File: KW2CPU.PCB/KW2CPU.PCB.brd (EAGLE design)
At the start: 31 x 17 mm, 25 parts, among them IC1 AT45DB161D8S1

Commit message: LasCon, KW2 Frontend
Exported LasCon for Jeff, made "wide" version for milling test.
Schematic for KW2 front end in progress, missing F and ant connector.
Updated KW2 and GW libs with frontend parts
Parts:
- added C$10, C$9, L$6, R$4, R$5, R$7, R$8: (no value), GW-devices:RF-L0201
- added C$13, C$15, C$16, C$18, C$20, C$21, C$22, C$24, L$11, L$14, L$17, R$12, R$19, R$23: (no value), GW-devices:RFMD0402
- added U$3: RF6555, KW2:RF6555
- moved U$1 13.6 mm to (51.6, 37.1)
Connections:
- new net N$19: R$7.P$2, U$3.P$5
- new net N$2: R$5.P$1, U$1.P$49
- new net N$20: R$8.P$2, U$3.P$6
- new net N$21: C$13.P$1, L$14.P$1, U$3.P$15
- new net N$22: C$10.P$1, C$9.P$2, L$11.P$1, U$3.P$10, U$3.P$8
- new net N$23: C$15.P$1, L$14.P$2
- new net N$24: C$18.P$1, L$17.P$2, U$3.P$17
- new net N$25: C$16.P$1, L$17.P$1
- new net N$26: R$19.P$2, U$1.P$44
- new net N$27: C$20.P$2, R$19.P$1, U$3.P$20
- new net N$29: R$12.P$1, U$3.P$23
- new net N$3: R$4.P$1, U$1.P$50
- new net N$30: C$24.P$1, R$23.P$1, U$1.P$46, U$3.P$2
- new net N$31: C$22.P$2, U$1.P$47, U$3.P$24
- new net N$4: L$6.P$2, R$4.P$2, R$7.P$1
- new net N$5: L$6.P$1, R$5.P$2, R$8.P$1
- net +3V3: now also C$21.P$1, L$11.P$2, U$3.P$22
- net GND: now also C$10.P$2, C$13.P$2, C$15.P$2, C$16.P$2, C$18.P$2, C$20.P$1, C$21.P$2, C$22.P$1, C$24.P$2, C$9.P$1, R$12.P$2, U$3.P$1, U$3.P$12, U$3.P$13, U$3.P$14, U$3.P$16, U$3.P$18, U$3.P$19, U$3.P$3, U$3.P$7, U$3.P$9
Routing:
- net +3V3: track 33.3 -> 0.00 mm
- net GND: track 28.2 -> 0.00 mm
- net N$14: track 20.8 -> 0.00 mm
- net N$10: track 11.8 -> 0.00 mm
- net N$7: track 9.85 -> 0.00 mm
- net CLKM1: track 9.62 -> 0.00 mm
- net N$18: track 9.49 -> 0.00 mm
- net N$16: track 6.98 -> 0.00 mm
- net N$13: track 19.8 -> 14.4 mm, vias 1 -> 0
- net N$17: track 4.81 -> 0.00 mm
- net N$6: track 4.15 -> 0.00 mm
- net CLKM2: track 4.05 -> 0.00 mm
- net N$8: track 3.74 -> 0.00 mm
- net N$12: track 16.8 -> 14.4 mm, vias 1 -> 0
- net N$9: track 2.41 -> 0.00 mm
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
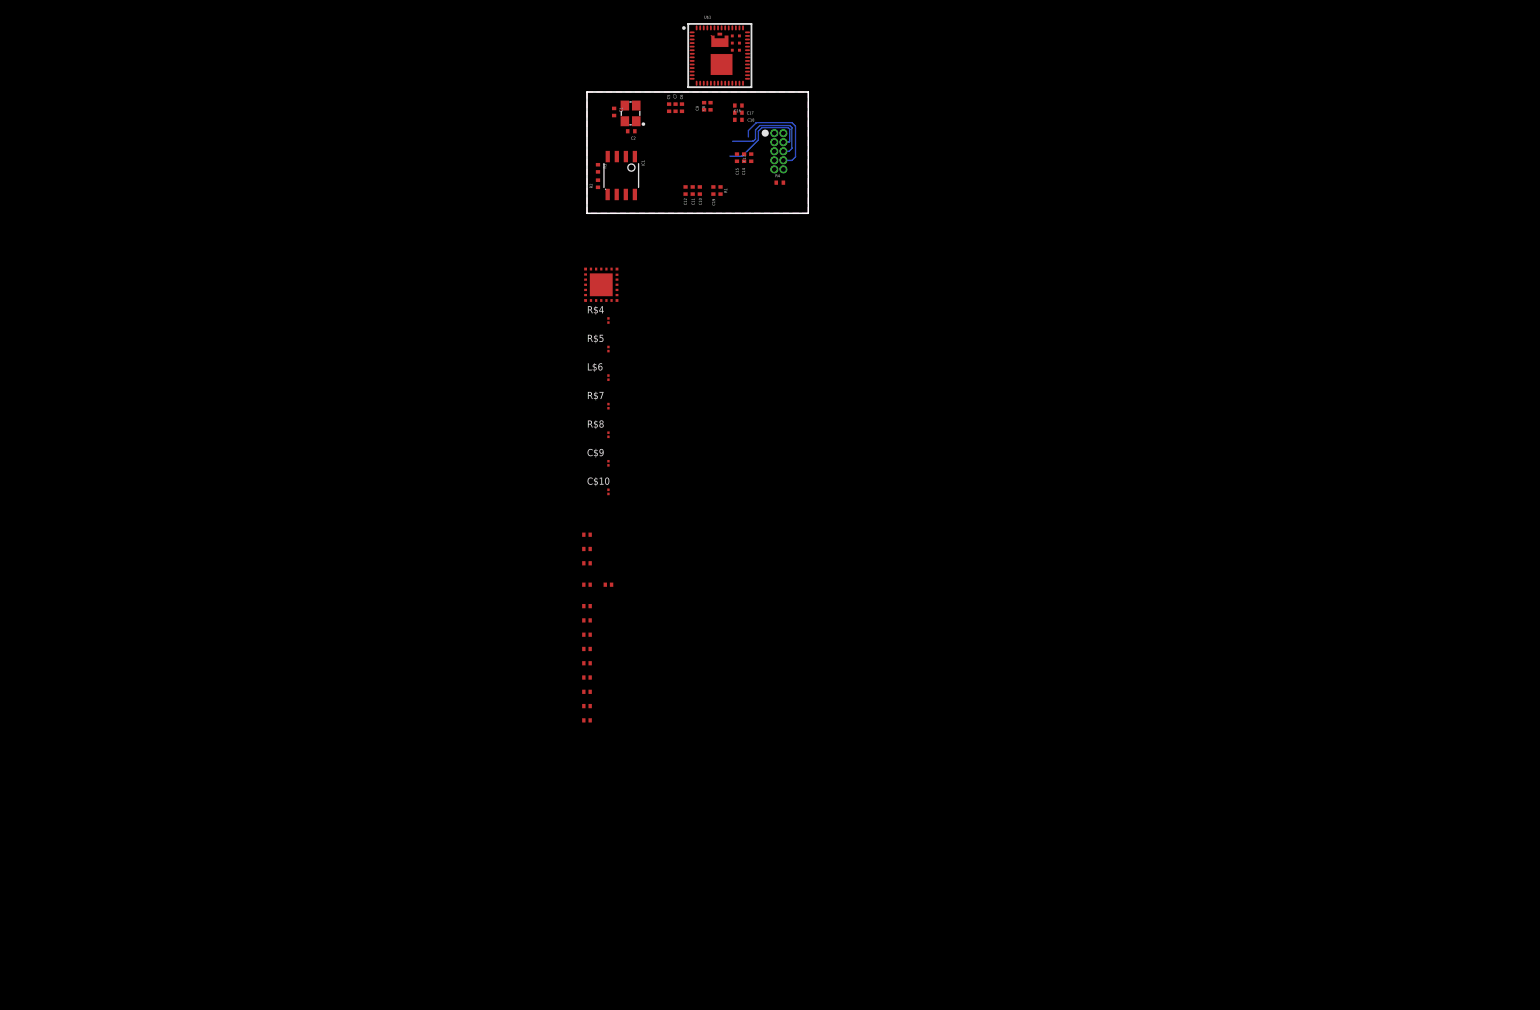
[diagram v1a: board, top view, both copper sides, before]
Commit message: KW2 antenna, LasCon panel, PosCon fiducials
Added vertical MMCX connector to KW2 design & library; added panelized
version of LasCon (old and new design); added Adafruit library and
fiducials to new PosCon
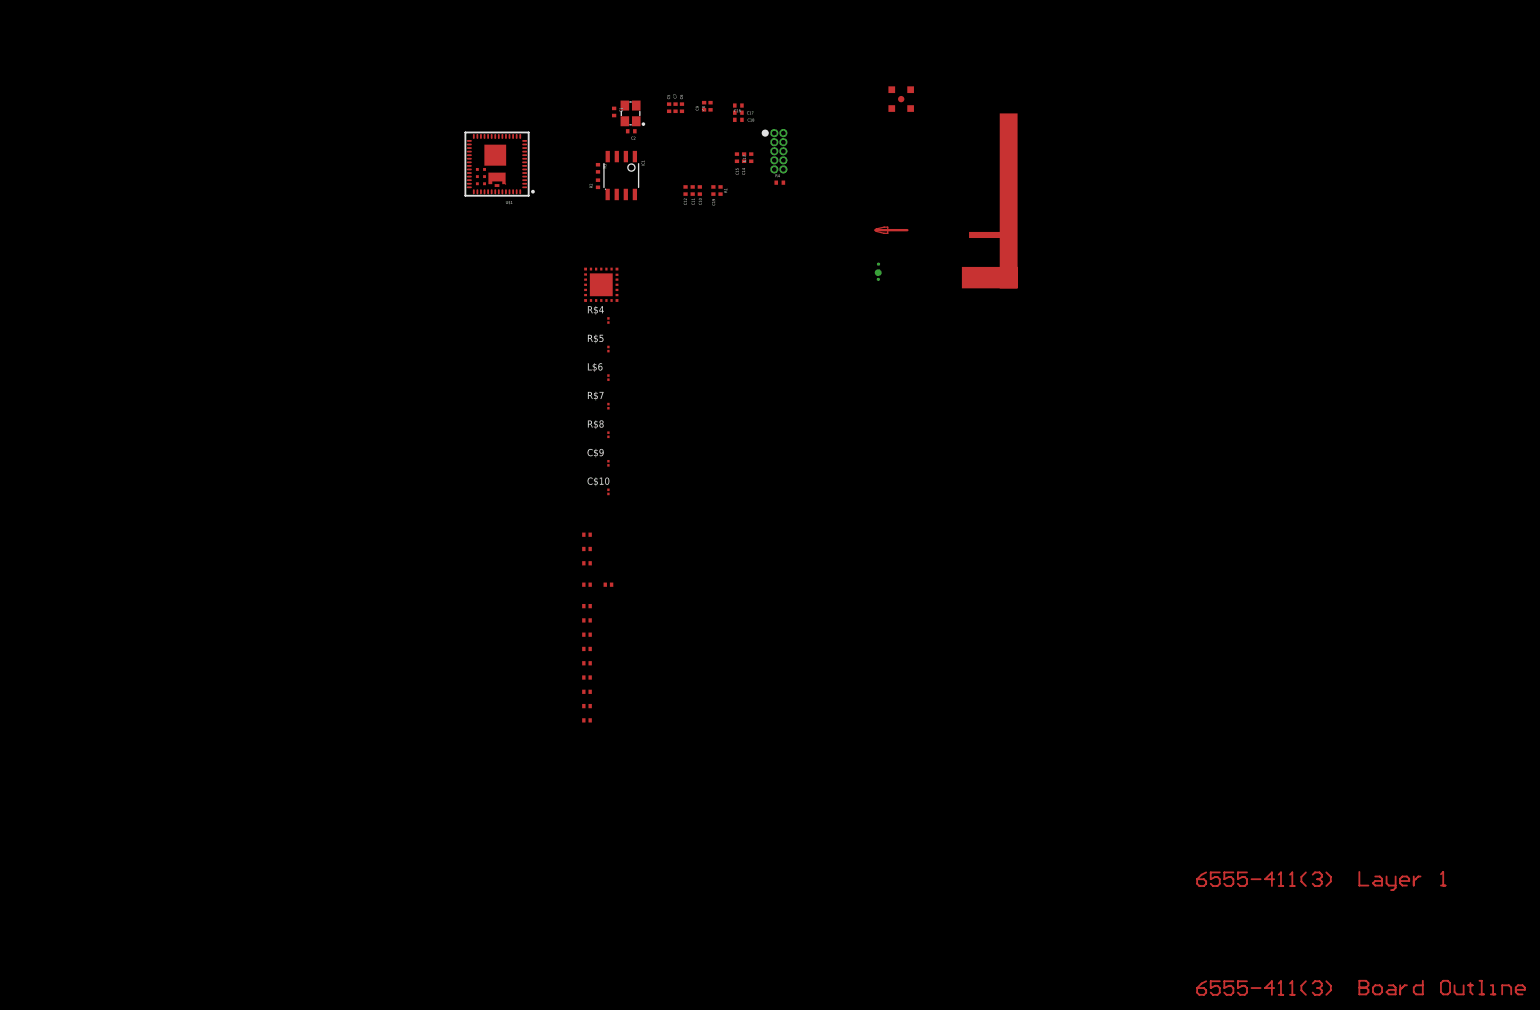
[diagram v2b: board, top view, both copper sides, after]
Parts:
- added U$4: F-ANTENNA-4LTOP, GW-devices:F-ANTENNA-4LAYER-TOP
- added U$5: MMCX_VERT, KW2:MMCX_VERT
- moved U$1 24.3 mm to (28.4, 29.9), turned to 180 degrees
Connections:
- net GND: now also U$4.GND, U$5.P$2, U$5.P$3, U$5.P$4, U$5.P$5
- net N$23: now also U$4.IN
- net N$25: now also U$5.P$1
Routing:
- net N$12: track 14.4 -> 0.00 mm
- net N$13: track 14.4 -> 0.00 mm
- net N$11: track 13.5 -> 0.00 mm
- net 1_9: track 0.00 -> 4.51 mm
- net 1_79: track 0.00 -> 4.50 mm
- net 1_83: track 0.00 -> 1.91 mm
- net 1_303: track 0.00 -> 1.91 mm
- net 1_299: track 0.00 -> 1.91 mm
- net 1_294: track 0.00 -> 1.91 mm
- net 1_239: track 0.00 -> 1.91 mm
- net 1_213: track 0.00 -> 1.91 mm
- net 1_182: track 0.00 -> 1.91 mm
- net 1_162: track 0.00 -> 1.91 mm
- net 1_158: track 0.00 -> 1.91 mm
- net 1_153: track 0.00 -> 1.91 mm
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- removed copper zone on layer 1, net GND
- removed copper zone on layer 16, net GND
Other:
- board outline removed

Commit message: PosCon parts, KW2 frontend, LasCon
Added part numbers for orange display, black buttons to PosCon. Worked
on frontend layout for KW2 and produced a new version of LasCon
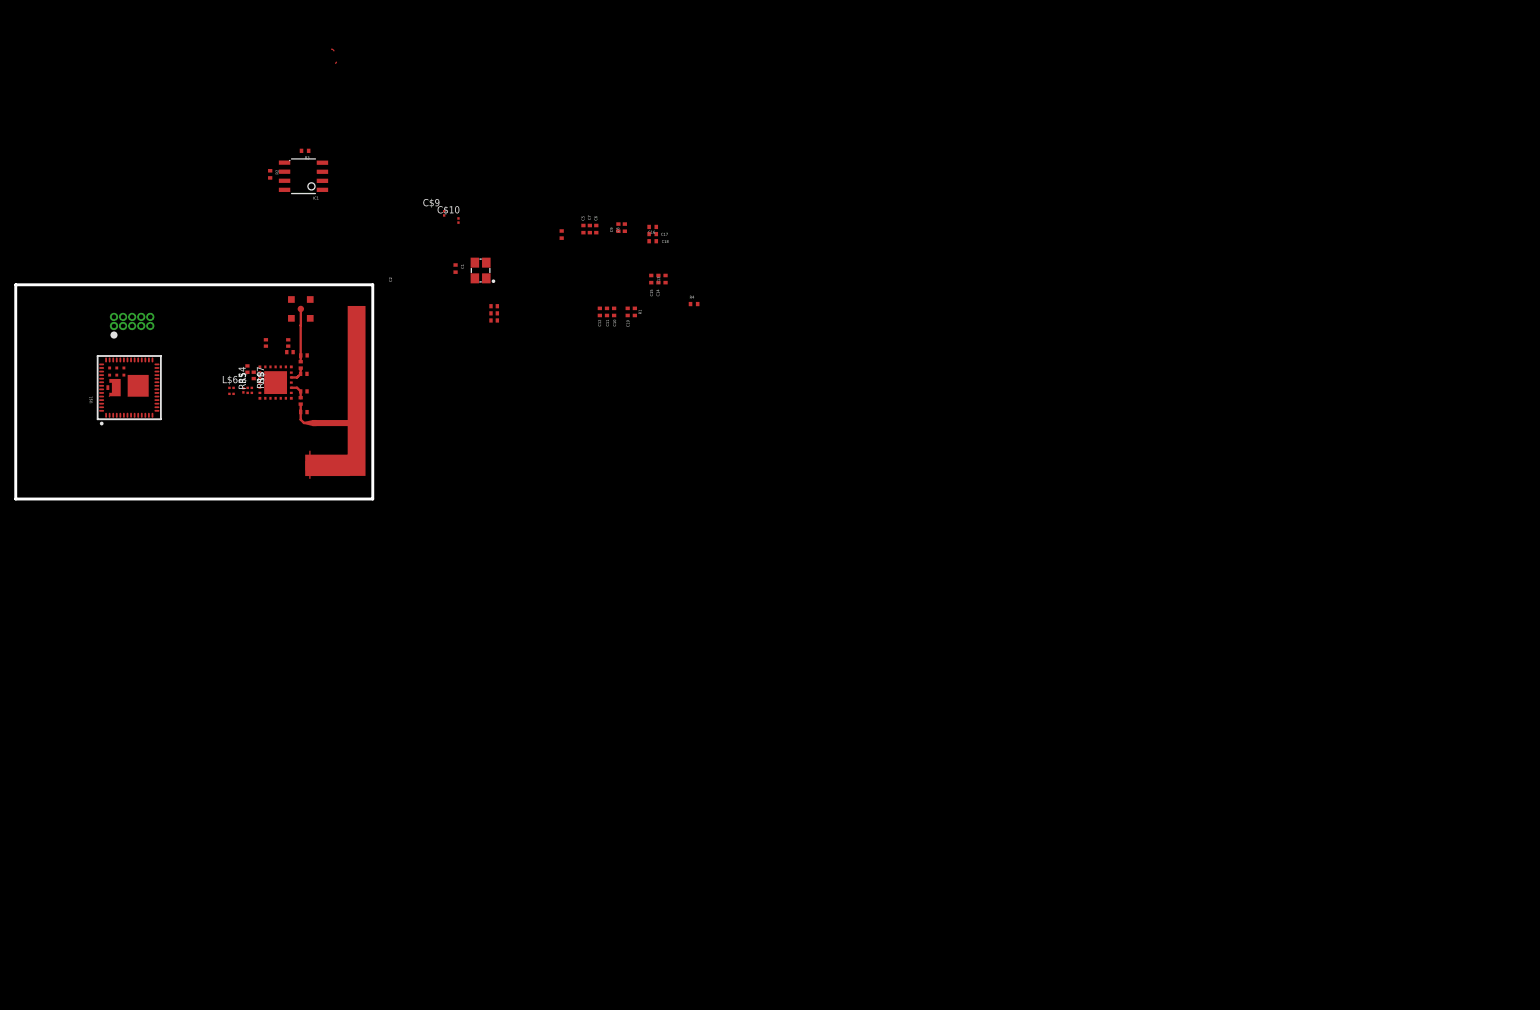
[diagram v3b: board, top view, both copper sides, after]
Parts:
- U$4: value F-ANTENNA-4LTOP -> F-ANTENNA; device GW-devices:F-ANTENNA-4LAYER-TOP -> KW2:F_ANT_RFMD
- moved JP1 94.1 mm to (-26.7, 4.50), turned to 0 degrees
- moved U$4 93.3 mm to (1.28, -13.0), turned to 0 degrees
- moved U$5 89.1 mm to (-3.08, 5.62)
- moved C$24 68.4 mm to (-10.6, -2.81), turned to 90 degrees
- moved R$23 65.7 mm to (-9.67, -3.69), turned to 270 degrees
- moved U$1 64.8 mm to (-23.1, -9.40), turned to 90 degrees
- moved R$12 63.5 mm to (-7.96, 0.85), turned to 90 degrees
- moved C$20 57.4 mm to (-4.60, -0.43), turned to 180 degrees
- moved R$19 57.1 mm to (-4.84, 0.85), turned to 90 degrees
- moved R$4 53.6 mm to (-12.8, -5.44), turned to 270 degrees
- moved C$22 53.6 mm to (24.0, 4.00)
- moved R$5 53.2 mm to (-12.8, -6.27), turned to 270 degrees
- moved L$17 53.0 mm to (-3.09, -2.22), turned to 270 degrees
- moved C$21 52.6 mm to (24.0, 5.00)
- moved C$18 51.3 mm to (-2.66, -3.48)
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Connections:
- net GND: now also U$4.P$2; no longer U$4.GND
- net N$23: now also U$4.P$1; no longer U$4.IN
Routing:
- net N$25: track 0.00 -> 7.42 mm
- net 1_9: track 4.51 -> 0.00 mm
- net 1_79: track 4.50 -> 0.00 mm
- net N$23: track 0.00 -> 2.84 mm
- net N$21: track 0.00 -> 2.48 mm
- net N$24: track 0.00 -> 2.33 mm
- net 1_83: track 1.91 -> 0.00 mm
- net 1_303: track 1.91 -> 0.00 mm
- net 1_299: track 1.91 -> 0.00 mm
- net 1_294: track 1.91 -> 0.00 mm
- net 1_239: track 1.91 -> 0.00 mm
- net 1_213: track 1.91 -> 0.00 mm
- net 1_182: track 1.91 -> 0.00 mm
- net 1_162: track 1.91 -> 0.00 mm
- net 1_158: track 1.91 -> 0.00 mm
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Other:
- board outline added: 50 x 30 mm

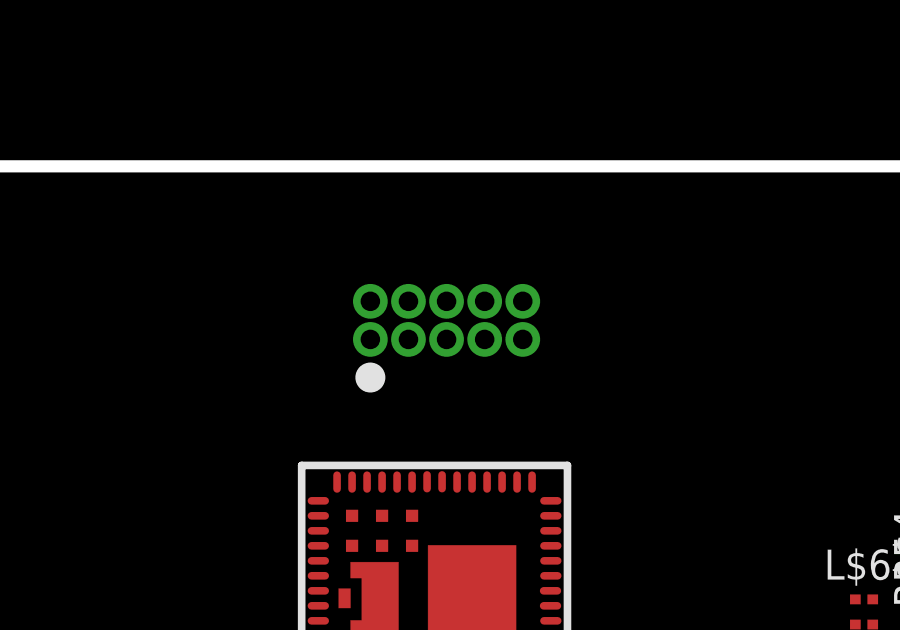
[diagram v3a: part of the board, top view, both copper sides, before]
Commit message: Added DF12 connector, moved PosCon
Still need device for DF12_F, moved PosCon.PCB to own repo
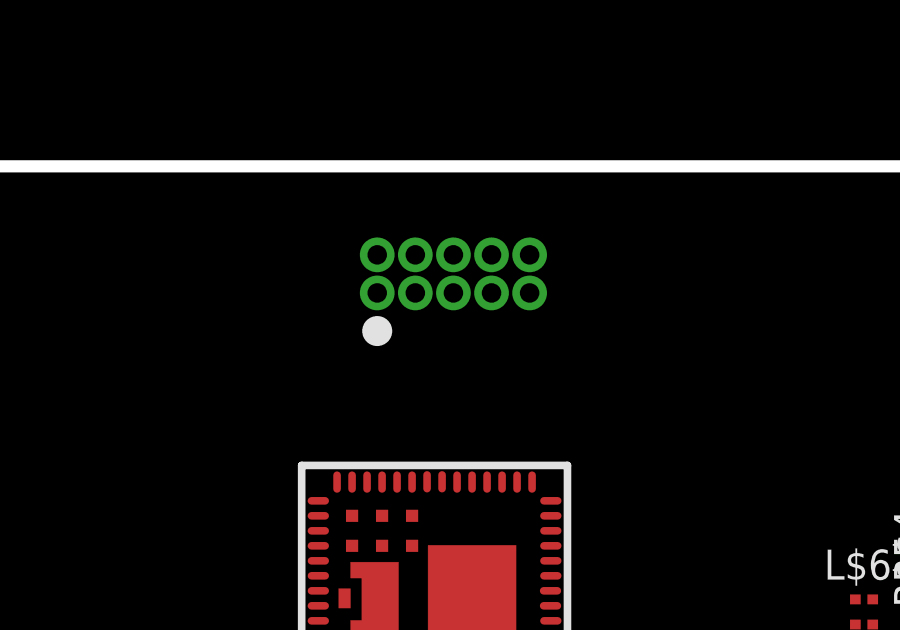
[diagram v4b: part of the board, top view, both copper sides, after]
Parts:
- moved JP1 1.57 mm to (-26.5, 6.05)
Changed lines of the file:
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@@
 <attribute name="VALUE" x="-1.843921875" y="29.7901625" size="1.27" layer="27" rot="R180"/>
 </element>
-<element name="JP1" library="KW2" package="2X5HDR" value="" x="-26.7" y="4.5" smashed="yes"/>
+<element name="JP1" library="KW2" package="2X5HDR" value="" x="-26.4714" y="6.0494" smashed="yes"/>
 <element name="R4" library="GW-devices" package="RF-R0402" value="10k" x="52" y="6.3" smashed="yes">
 <attribute name="NAME" x="51.365" y="7.062" size="0.4064" layer="25"/>
@@
 <wire x1="-30.975" y1="-6.15" x2="-30.1" y2="-5.4" width="0" layer="19" extent="1-1"/>
 <wire x1="-30.974" y1="-4.649" x2="-30.1" y2="-5.4" width="0" layer="19" extent="1-1"/>
-<wire x1="-26.7" y1="3.23" x2="-23.225" y2="-2.15" width="0" layer="19" extent="1-1"/>
-<wire x1="-27.97" y1="3.23" x2="-26.7" y2="3.23" width="0" layer="19" extent="1-1"/>
+<wire x1="-26.4714" y1="4.7794" x2="-23.225" y2="-2.15" width="0" layer="19" extent="1-1"/>
+<wire x1="-27.7414" y1="4.7794" x2="-26.4714" y2="4.7794" width="0" layer="19" extent="1-1"/>
 <wire x1="-5.354" y1="23.565" x2="-4.3962" y2="6.939" width="0" layer="19" extent="1-1"/>
 </signal>
@@
 <wire x1="-30.35" y1="-1.525" x2="-28.35" y2="-1.525" width="0" layer="19" extent="1-1"/>
 <wire x1="-30.975" y1="-2.15" x2="-30.35" y2="-1.525" width="0" layer="19" extent="1-1"/>
-<wire x1="-29.24" y1="3.23" x2="-28.35" y2="-1.525" width="0" layer="19" extent="1-1"/>
+<wire x1="-29.0114" y1="4.7794" x2="-28.35" y2="-1.525" width="0" layer="19" extent="1-1"/>
 <wire x1="-30.975" y1="-8.15" x2="-30.975" y2="-2.15" width="0" layer="19" extent="1-1"/>
 <wire x1="-7.366575" y1="23.965303125" x2="-6.60679375" y2="-2.497475" width="0" layer="19" extent="1-1"/>
@@
 <contactref element="U$1" pad="P$36"/>
 <contactref element="JP1" pad="P$2"/>
-<wire x1="-29.24" y1="4.5" x2="-27.35" y2="-1.515" width="0" layer="19" extent="1-1"/>
+<wire x1="-29.0114" y1="6.0494" x2="-27.35" y2="-1.515" width="0" layer="19" extent="1-1"/>
 </signal>
 <signal name="N$11">
 <contactref element="U$1" pad="P$33"/>
 <contactref element="JP1" pad="P$4"/>
-<wire x1="-27.97" y1="4.5" x2="-25.85" y2="-1.525" width="0" layer="19" extent="1-1"/>
+<wire x1="-27.7414" y1="6.0494" x2="-25.85" y2="-1.525" width="0" layer="19" extent="1-1"/>
 </signal>
 <signal name="N$12">
 <contactref element="U$1" pad="P$35"/>
 <contactref element="JP1" pad="P$6"/>
-<wire x1="-26.7" y1="4.5" x2="-26.85" y2="-1.515" width="0" layer="19" extent="1-1"/>
+<wire x1="-26.4714" y1="6.0494" x2="-26.85" y2="-1.515" width="0" layer="19" extent="1-1"/>
 </signal>
 <signal name="N$13">
 <contactref element="U$1" pad="P$34"/>
 <contactref element="JP1" pad="P$8"/>
-<wire x1="-25.43" y1="4.5" x2="-26.35" y2="-1.525" width="0" layer="19" extent="1-1"/>
+<wire x1="-25.2014" y1="6.0494" x2="-26.35" y2="-1.525" width="0" layer="19" extent="1-1"/>
 </signal>
 <signal name="N$14">
 <contactref element="JP1" pad="P$10"/>
 <contactref element="U$1" pad="P$41"/>
-<wire x1="-24.16" y1="4.5" x2="-29.85" y2="-1.525" width="0" layer="19" extent="1-1"/>
+<wire x1="-23.9314" y1="6.0494" x2="-29.85" y2="-1.525" width="0" layer="19" extent="1-1"/>
 </signal>
 <signal name="N$15">
 <contactref element="R4" pad="1"/>
 <contactref element="JP1" pad="P$9"/>
-<wire x1="-24.16" y1="3.23" x2="51.5" y2="6.3" width="0" layer="19" extent="1-1"/>
+<wire x1="-23.9314" y1="4.7794" x2="51.5" y2="6.3" width="0" layer="19" extent="1-1"/>
 </signal>
 <signal name="N$7">
